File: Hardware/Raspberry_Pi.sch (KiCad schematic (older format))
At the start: 21 parts, among them J1 M20-9762042, J2 Motor_2, J3 Motor_1, J8 FTDI, Q2 DMG2301L, Q3 DMG3414U, Q4 DMG2301L, Q5 DMG3414U

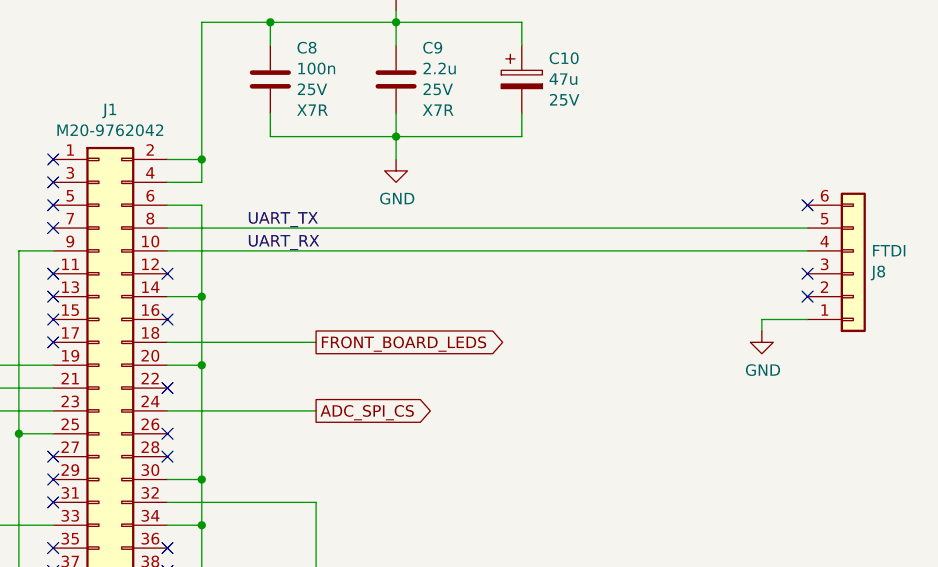
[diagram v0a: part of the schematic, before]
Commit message: [Hardware] Added lidar support to schematic.
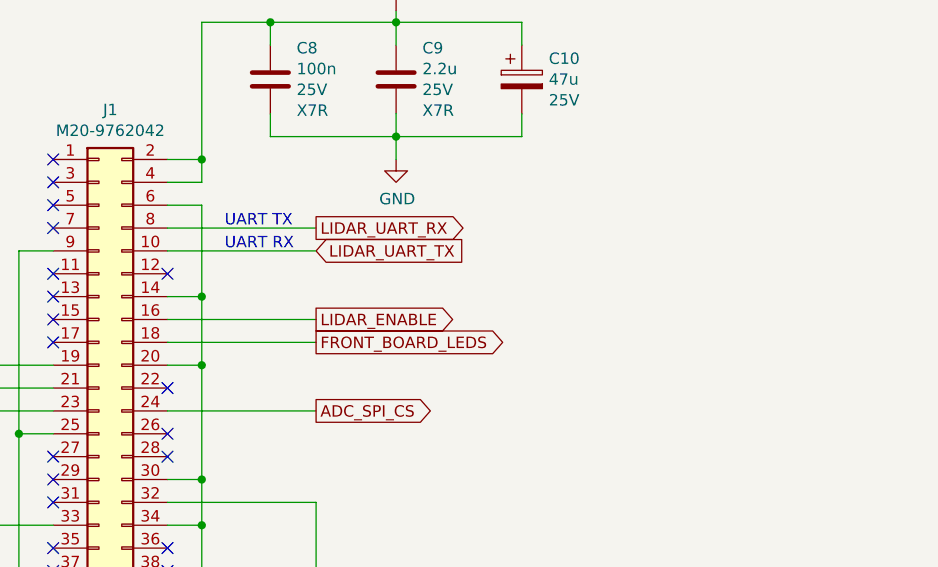
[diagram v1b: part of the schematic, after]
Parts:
- removed J8: FTDI, Connector_PinHeader_2.54mm:PinHeader_1x06_P2.54mm_Horizontal, symbol Connector_Generic:Conn_01x06
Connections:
- net LIDAR_ENABLE: now reaches J1.16 (Pin_16)
- net UART_RX renamed LIDAR_UART_TX
- net UART_TX renamed LIDAR_UART_RX
- no-connect marks 24 -> 20
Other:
- note added: "UART RX"
- note added: "UART TX"

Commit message: [Hardware] Indicated all mechanical parts that must not be populated.
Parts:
- C15, C16: ManufacturerReference CC1206KRX7R9BB104 -> (none)
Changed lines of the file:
@@
 F 4 "25V" H 1985 6595 50  0000 R CNN "Value2"
 F 5 "X7R" H 1985 6686 50  0000 R CNN "Value3"
-F 6 "CC1206KRX7R9BB104" V 2100 6550 50  0001 C CNN "ManufacturerReference"
 	1    2100 6550
 	1    0    0    1
@@
 F 4 "25V" H 1985 4095 50  0000 R CNN "Value2"
 F 5 "X7R" H 1985 4186 50  0000 R CNN "Value3"
-F 6 "CC1206KRX7R9BB104" V 2100 4050 50  0001 C CNN "ManufacturerReference"
 	1    2100 4050
 	1    0    0    1
